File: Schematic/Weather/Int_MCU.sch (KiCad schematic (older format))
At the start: 7 parts, among them U1 AMS1117, U2 ESP-01v090

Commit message: North TxRx diode change
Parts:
- R2: value 10k -> 4.7K
- U2: symbol ESP8266:ESP-01v090 -> Weather-rescue:ESP-01v090-ESP8266
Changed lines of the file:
@@
 J3_P4
 $Comp
-L ESP8266:ESP-01v090 U2
+L Weather-rescue:ESP-01v090-ESP8266 U2
 U 1 1 5C9306F6
 P 5800 2650
+AR Path="/5C9306F6" Ref="U2"  Part="1"
+AR Path="/5C9253D5/5C9306F6" Ref="U2"  Part="1"
 F 0 "U2" H 5800 3165 50  0000 C CNN
 F 1 "ESP-01v090" H 5800 3074 50  0000 C CNN
@@
 P 4300 2450
 F 0 "R2" H 4370 2496 50  0000 L CNN
-F 1 "10k" H 4370 2405 50  0000 L CNN
+F 1 "4.7K" H 4370 2405 50  0000 L CNN
 F 2 "Resistor_THT:R_Axial_DIN0207_L6.3mm_D2.5mm_P7.62mm_Horizontal" V 4230 2450 50  0001 C CNN
 F 3 "~" H 4300 2450 50  0001 C CNN

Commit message: Start PCB
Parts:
- C1, C3: footprint (none) -> Capacitor_THT:CP_Radial_Tantal_D7.0mm_P5.00mm
- C2: footprint (none) -> Capacitor_THT:C_Disc_D3.8mm_W2.6mm_P2.50mm
- U1: footprint (none) -> Package_TO_SOT_SMD:SOT-223-3_TabPin2
- U2: footprint (none) -> footprint:ESP-01
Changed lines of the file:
@@
 F 0 "U2" H 5800 3165 50  0000 C CNN
 F 1 "ESP-01v090" H 5800 3074 50  0000 C CNN
-F 2 "" H 5800 2650 50  0001 C CNN
+F 2 "footprint:ESP-01" H 5800 2650 50  0001 C CNN
 F 3 "http://l0l.org.uk/2014/12/esp8266-modules-hardware-guide-gotta-catch-em-all/" H 5800 2650 50  0001 C CNN
 	1    5800 2650
@@
 F 0 "U1" V 2600 1550 60  0000 L CNN
 F 1 "AMS1117" V 3600 1400 60  0000 L CNN
-F 2 "" H 3100 1600 60  0000 C CNN
+F 2 "Package_TO_SOT_SMD:SOT-223-3_TabPin2" H 3100 1600 60  0001 C CNN
 F 3 "" H 3100 1600 60  0000 C CNN
 	1    3100 1600
@@
 F 0 "C2" H 4065 3246 50  0000 L CNN
 F 1 "0.1uF" H 4065 3155 50  0000 L CNN
-F 2 "" H 3988 3050 50  0001 C CNN
+F 2 "Capacitor_THT:C_Disc_D3.8mm_W2.6mm_P2.50mm" H 3988 3050 50  0001 C CNN
 F 3 "~" H 3950 3200 50  0001 C CNN
 	1    3950 3200
@@
 F 0 "C1" H 2618 2746 50  0000 L CNN
 F 1 "47uF" H 2618 2655 50  0000 L CNN
-F 2 "" H 2538 2550 50  0001 C CNN
+F 2 "Capacitor_THT:CP_Radial_Tantal_D7.0mm_P5.00mm" H 2538 2550 50  0001 C CNN
 F 3 "~" H 2500 2700 50  0001 C CNN
 	1    2500 2700
@@
 F 0 "C3" H 4468 3246 50  0000 L CNN
 F 1 "47uF" H 4468 3155 50  0000 L CNN
-F 2 "" H 4388 3050 50  0001 C CNN
+F 2 "Capacitor_THT:CP_Radial_Tantal_D7.0mm_P5.00mm" H 4388 3050 50  0001 C CNN
 F 3 "~" H 4350 3200 50  0001 C CNN
 	1    4350 3200

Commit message: Borad layout 2x for Tx Rx
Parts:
- C1, C3: footprint Capacitor_THT:CP_Radial_Tantal_D7.0mm_P5.00mm -> Capacitor_THT:CP_Radial_Tantal_D5.0mm_P2.50mm
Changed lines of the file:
@@
 F 0 "C1" H 2618 2746 50  0000 L CNN
 F 1 "47uF" H 2618 2655 50  0000 L CNN
-F 2 "Capacitor_THT:CP_Radial_Tantal_D7.0mm_P5.00mm" H 2538 2550 50  0001 C CNN
+F 2 "Capacitor_THT:CP_Radial_Tantal_D5.0mm_P2.50mm" H 2538 2550 50  0001 C CNN
 F 3 "~" H 2500 2700 50  0001 C CNN
 	1    2500 2700
@@
 F 0 "C3" H 4468 3246 50  0000 L CNN
 F 1 "47uF" H 4468 3155 50  0000 L CNN
-F 2 "Capacitor_THT:CP_Radial_Tantal_D7.0mm_P5.00mm" H 4388 3050 50  0001 C CNN
+F 2 "Capacitor_THT:CP_Radial_Tantal_D5.0mm_P2.50mm" H 4388 3050 50  0001 C CNN
 F 3 "~" H 4350 3200 50  0001 C CNN
 	1    4350 3200

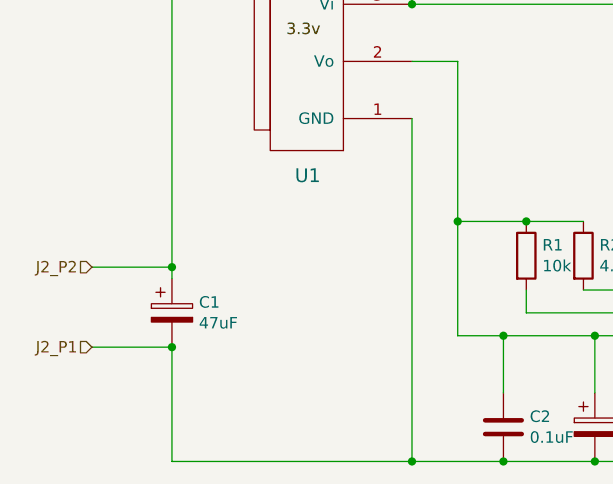
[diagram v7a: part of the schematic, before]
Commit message: Board update 4 channels
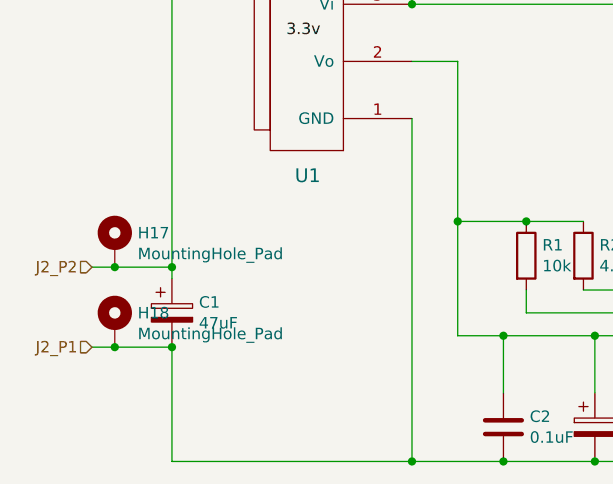
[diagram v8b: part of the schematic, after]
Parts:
- added H17, H18: MountingHole_Pad, symbol Mechanical:MountingHole_Pad
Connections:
- net J2_P1: now also H18.1
- net J2_P2: now also H17.1
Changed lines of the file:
@@
 	8150 2650 8350 2650
 Wire Wire Line
-	2150 2850 2500 2850
+	2150 2850 2250 2850
 Wire Wire Line
 	2500 2850 2500 3350
@@
 $EndComp
 Wire Wire Line
-	2150 2500 2500 2500
+	2150 2500 2250 2500
 $Comp
 L Device:CP C1
@@
 Text Label 8200 2950 0    50   ~ 0
 GND
+$Comp
+L Mechanical:MountingHole_Pad H17
+U 1 1 5CAD0AF5
+P 2250 2400
+F 0 "H17" H 2350 2449 50  0000 L CNN
+F 1 "MountingHole_Pad" H 2350 2358 50  0000 L CNN
+F 2 "" H 2250 2400 50  0001 C CNN
+F 3 "~" H 2250 2400 50  0001 C CNN
+	1    2250 2400
+	1    0    0    -1
+$EndComp
+$Comp
+L Mechanical:MountingHole_Pad H18
+U 1 1 5CAD120E
+P 2250 2750
+F 0 "H18" H 2350 2799 50  0000 L CNN
+F 1 "MountingHole_Pad" H 2350 2708 50  0000 L CNN
+F 2 "" H 2250 2750 50  0001 C CNN
+F 3 "~" H 2250 2750 50  0001 C CNN
+	1    2250 2750
+	1    0    0    -1
+$EndComp
+Connection ~ 2250 2850
+Wire Wire Line
+	2250 2850 2500 2850
+Connection ~ 2250 2500
+Wire Wire Line
+	2250 2500 2500 2500
 $EndSCHEMATC
